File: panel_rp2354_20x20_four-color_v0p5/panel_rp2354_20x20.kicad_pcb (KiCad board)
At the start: 6 copper layers, 45 x 45 mm, 557 parts, among them J1 Conn_01x04, J2 Conn_01x05, J3 Conn_01x05, J4 Conn_01x05, J5 Conn_01x05, SW1 SW_Push, SW2 SW_Push, U1 APS6404L-3SQR, U10 UCC27517, U11 UCC27517, U12 UCC27517, U13 UCC27517, U14 UCC27517, U15 UCC27517, U16 UCC27517, U17 UCC27517, U18 UCC27517, U19 UCC27517, U2 RP2354B_80QFN, U20 UCC27517, U21 UCC27517, U22 UCC27517, U23 UCC27517, U24 UCC27517, U25 UCC27517, U26 UCC27517, U27 UCC27517, U28 UCC27517, U29 UCC27517, U3 UCC27517, U30 UCC27517, U31 UCC27517, U32 UCC27517, U33 UCC27517, U34 UCC27517, U35 UCC27517, U36 UCC27517, U37 UCC27517, U38 UCC27517, U39 UCC27517, U4 UCC27517, U40 UCC27517, U41 UCC27517, U42 UCC27517, U43 AP2112K-3.3, U5 UCC27517, U6 UCC27517, U7 UCC27517, U8 UCC27517, U9 UCC27517, Y1 ABM8-272-T3

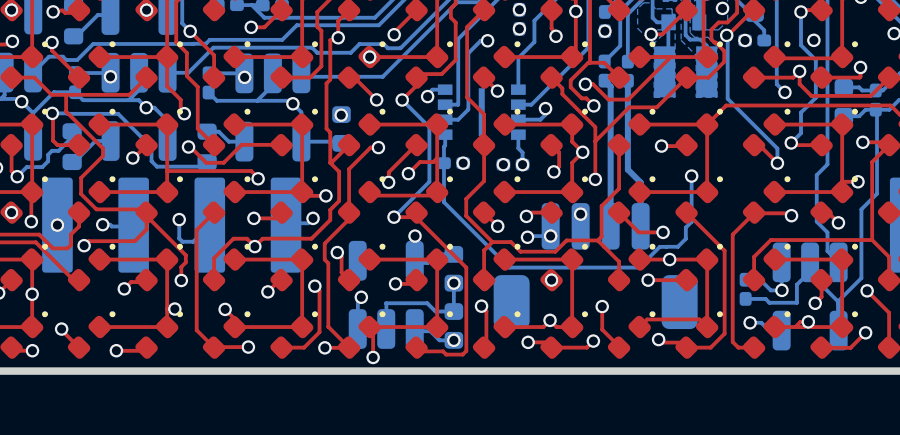
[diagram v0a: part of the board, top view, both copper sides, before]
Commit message: improve silkscreen
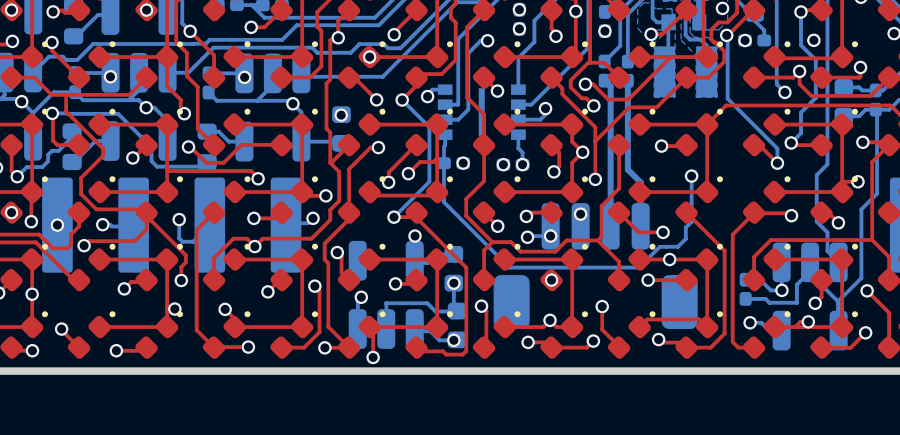
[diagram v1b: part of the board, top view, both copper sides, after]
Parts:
- moved C67 0.11 mm to (67.9, 93.5)
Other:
- board text added: "LED0: YY0402PU-NN LED1: YY0402BL-NN LED2: YY0402YE-RN LED3: YY0402RE-RN"
- board text added: "R0 R1: 68Ω ±0.1% R2 R3: 110Ω ±0.1%"
- board text removed: "LED0: YY0402PU LED1: YY0402BL LED2: YY0402GR LED3: YY0402YE"
- board text removed: "R[0|1|2]: 68Ω ±1% R3: 110Ω ±1%"
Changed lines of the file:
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@@
 	(paper "A4")
 	(title_block
-		(title "G6 PBGY 45mm RP2354")
-		(date "2026-08-26")
-		(rev "v0.4.0")
+		(title "G6 PBYR 45mm RP2354")
+		(date "2026-10-20")
+		(rev "v0.5.0")
 		(company "Reiserlab @ Janelia")
 	)
@@
 			(at 0 1.17 90)
 			(layer "B.SilkS")
+			(hide yes)
 			(effects
 				(font
@@
 			(at 0 1.17 90)
 			(layer "B.SilkS")
+			(hide yes)
 			(effects
 				(font
@@
 			(at 0 1.17 90)
 			(layer "B.SilkS")
+			(hide yes)
 			(effects
 				(font
@@
 			(at 0 1.17 90)
 			(layer "B.SilkS")
+			(hide yes)
 			(effects
 				(font
@@
 			(at 0 1.17 90)
 			(layer "B.SilkS")
+			(hide yes)
 			(effects
 				(font
@@
 			(at 0 1.17 90)
 			(layer "B.SilkS")
+			(hide yes)
 			(effects
 				(font
@@
 			(at 0 1.17 90)
 			(layer "B.SilkS")
+			(hide yes)
 			(effects
 				(font
@@
 			(at 0 1.17 90)
 			(layer "B.SilkS")
+			(hide yes)
 			(effects
 				(font
@@
 			(at 0 1.17 90)
 			(layer "B.SilkS")
+			(hide yes)
 			(effects
 				(font
@@
 			(at 0 1.17 90)
 			(layer "B.SilkS")
+			(hide yes)
 			(effects
 				(font
@@
 			(at 0 1.17 90)
 			(layer "B.SilkS")
+			(hide yes)
 			(effects
 				(font
@@
 			(at 0 1.17 90)
 			(layer "B.SilkS")
+			(hide yes)
 			(effects
 				(font
@@
 			(at 0 1.17 90)
 			(layer "B.SilkS")
+			(hide yes)
 			(effects
 				(font
@@
 			(at 0 1.17 90)
 			(layer "B.SilkS")
+			(hide yes)
 			(effects
 				(font
@@
 			(at 0 1.17 90)
 			(layer "B.SilkS")
+			(hide yes)
 			(effects
 				(font
@@
 			(at 0 1.17 90)
 			(layer "B.SilkS")
+			(hide yes)
 			(effects
 				(font
@@
 	(footprint "Capacitor_SMD:C_0402_1005Metric"
 		(layer "B.Cu")
-		(at 67.775 93.495 90)
+		(at 67.88 93.48 90)
 		(descr "Capacitor SMD 0402 (1005 Metric), square (rectangular) end terminal, IPC-7351 nominal, (Body size source: IPC-SM-782 page 76, https://www.pcb-3d.com/wordpress/wp-content/uploads/ipc-sm-782a_amendment_1_and_2.pdf), generated with kicad-footprint-generator")
 		(tags "capacitor")
@@
 			(at 0 1.17 90)
 			(layer "B.SilkS")
+			(hide yes)
 			(effects
 				(font
@@
 			(at 0 1.17 90)
 			(layer "B.SilkS")
+			(hide yes)
 			(effects
 				(font
@@
 			(at 0 1.17 90)
 			(layer "B.SilkS")
+			(hide yes)
 			(effects
 				(font
@@
 			(at 0 1.17 90)
 			(layer "B.SilkS")
+			(hide yes)
 			(effects
 				(font
@@
 		(layer "Edge.Cuts")
 	)
-	(gr_text "R[0|1|2]: 68Ω ±1%\nR3:       110Ω ±1%"
-		(at 77.8 81.6 0)
+	(gr_text "R0 R1: 68Ω ±0.1%\nR2 R3: 110Ω ±0.1%"
+		(at 74.65 81.7 0)
 		(layer "B.SilkS")
 		(effects
@@
 		)
 	)
-	(gr_text "LED0: YY0402PU\nLED1: YY0402BL\nLED2: YY0402GR\nLED3: YY0402YE"
-		(at 77.6 70.4 0)
+	(gr_text "LED0: YY0402PU-NN\nLED1: YY0402BL-NN\nLED2: YY0402YE-RN\nLED3: YY0402RE-RN"
+		(at 77.175 70.58 0)
 		(layer "B.SilkS")
 		(effects
@@
 	)
 	(gr_text "0 1\n2 3"
-		(at 67.2 69.2 0)
+		(at 67.22 73.64 0)
 		(layer "B.SilkS" knockout)
 		(effects
@@
 	)
 	(gr_text "${TITLE}"
-		(at 80 85 90)
+		(at 79.74 84.99 90)
 		(layer "B.SilkS")
 		(effects
@@
 	)
 	(segment
-		(start 66.99 93.67)
-		(end 67.295 93.975)
-		(width 0.127)
-		(layer "B.Cu")
-		(net "+5V")
-	)
-	(segment
 		(start 51.85 85.12)
 		(end 50.665 85.12)
@@
 	)
 	(segment
+		(start 67.865 93.975)
+		(end 67.88 93.96)
+		(width 0.127)
+		(layer "B.Cu")
+		(net "+5V")
+	)
+	(segment
 		(start 81.87 63.495)
 		(end 82.67 63.495)
@@
 	)
 	(segment
-		(start 66.5425 93.67)
-		(end 66.99 93.67)
-		(width 0.127)
-		(layer "B.Cu")
-		(net "+5V")
-	)
-	(segment
 		(start 90.845 85.635)
 		(end 91.4175 85.0625)
@@
 	)
 	(segment
+		(start 66.99 93.67)
+		(end 67.295 93.975)
+		(width 0.127)
+		(layer "B.Cu")
+		(net "+5V")
+	)
+	(segment
 		(start 86.8 80.76)
 		(end 86.815 80.745)
@@
 	)
 	(segment
+		(start 66.5425 93.67)
+		(end 66.99 93.67)
+		(width 0.127)
+		(layer "B.Cu")
+		(net "+5V")
+	)
+	(segment
 		(start 69.2 52.59)
 		(end 69.2 53.56)
@@
 	)
 	(segment
+		(start 67.295 93.975)
+		(end 67.865 93.975)
+		(width 0.127)
+		(layer "B.Cu")
+		(net "+5V")
+	)
+	(segment
 		(start 65.1 60.055)
 		(end 65.605 60.055)
@@
 	)
 	(segment
-		(start 67.295 93.975)
-		(end 67.775 93.975)
-		(width 0.127)
-		(layer "B.Cu")
-		(net "+5V")
-	)
-	(segment
 		(start 51.89 63.73)
 		(end 52.502 63.118)
@@
 	)
 	(segment
+		(start 67.865 93.015)
+		(end 67.88 93)
+		(width 0.127)
+		(layer "B.Cu")
+		(net "GND")
+	)
+	(segment
 		(start 93.27 81.7)
 		(end 93.7875 82.2175)
@@
 	)
 	(segment
-		(start 67.165 93.015)
-		(end 67.775 93.015)
-		(width 0.127)
-		(layer "B.Cu")
-		(net "GND")
-	)
-	(segment
 		(start 57.06 77.7)
 		(end 57.35 77.7)
@@
 	)
 	(segment
+		(start 65.51 92.74)
+		(end 66.89 92.74)
+		(width 0.127)
+		(layer "B.Cu")
+		(net "GND")
+	)
+	(segment
 		(start 92.65 64.89)
 		(end 92.85 64.69)
@@
 	)
 	(segment
+		(start 67.775 92.895)
+		(end 67.775 92.07)
+		(width 0.127)
+		(layer "B.Cu")
+		(net "GND")
+	)
+	(segment
 		(start 53.75 69.41)
 		(end 52.8 68.46)
@@
 	)
 	(segment
+		(start 66.89 92.74)
+		(end 67.165 93.015)
+		(width 0.127)
+		(layer "B.Cu")
+		(net "GND")
+	)
+	(segment
 		(start 67.02 56.52)
 		(end 67.225 56.315)
@@
 	)
 	(segment
+		(start 67.88 93)
+		(end 67.775 92.895)
+		(width 0.127)
+		(layer "B.Cu")
+		(net "GND")
+	)
+	(segment
 		(start 89.28 83.02)
 		(end 89.28 82.04)
@@
 	)
 	(segment
-		(start 65.51 92.74)
-		(end 66.89 92.74)
-		(width 0.127)
-		(layer "B.Cu")
-		(net "GND")
-	)
-	(segment
 		(start 57.52 86.22)
 		(end 57.27 85.97)
@@
 	)
 	(segment
-		(start 67.775 93.015)
-		(end 67.775 92.07)
-		(width 0.127)
-		(layer "B.Cu")
-		(net "GND")
-	)
-	(segment
 		(start 83.76 69.02)
 		(end 82.15 69.02)
@@
 	)
 	(segment
+		(start 67.165 93.015)
+		(end 67.865 93.015)
+		(width 0.127)
+		(layer "B.Cu")
+		(net "GND")
+	)
+	(segment
 		(start 72.5 77.1333)
 		(end 73.6333 77.1333)
@@
 		(width 0.127)
 		(layer "B.Cu")
-		(net "GND")
-	)
-	(segment
-		(start 66.89 92.74)
-		(end 67.165 93.015)
-		(width 0.127)
-		(layer "B.Cu")

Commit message: add DBG connector
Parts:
- added J6: Conn_01x03, Connector_JST:JST_SH_BM03B-SRSS-TB_1x03-1MP_P1.00mm_Vertical, B.Cu at (77.9, 66.5)
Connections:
- U2 pad 33: unconnected-(U2-SWCLK-Pad33) -> Net-(J6-Pin_1)
- U2 pad 34: unconnected-(U2-SWD-Pad34) -> Net-(J6-Pin_3)
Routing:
- net Net-(J6-Pin_3): track 0.00 -> 8.96 mm
- net Net-(J6-Pin_1): track 0.00 -> 6.03 mm
- net Net-(D261-A): track 142.4 -> 147.9 mm
- net Net-(D221-A): track 133.3 -> 137.4 mm
- net Net-(D181-A): track 146.3 -> 149.4 mm
- net Net-(D281-A): track 126.1 -> 128.2 mm
- net Net-(D301-A): track 130.8 -> 132.8 mm
- net Net-(D241-A): track 144.1 -> 145.4 mm
- net /drivers/ROW_MCU_03: track 28.0 -> 27.0 mm
- net /drivers/ROW_15: track 86.7 -> 87.6 mm
- net /drivers/ROW_MCU_09: track 19.0 -> 18.4 mm
- net /drivers/ROW_MCU_07: track 17.5 -> 17.0 mm
- net GND: track 266.8 -> 266.6 mm, vias 68 -> 69
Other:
- board text added: "DBG"
- board text added: "USB"
- board text removed: "BOTTOM"
- board text removed: "TOP"
